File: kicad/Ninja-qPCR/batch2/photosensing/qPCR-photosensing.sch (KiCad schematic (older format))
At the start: 26 parts

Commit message: Add schematics
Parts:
- removed C? (x2): 0.1uF, symbol Device:C
- removed C?: 10pF, symbol Device:C
- removed C? (x2): 0.22uF, symbol Device:C
- removed R? (x2): 560, symbol Device:R
- removed R?: 1.1M, symbol Device:R
- removed R?: 1800, symbol Device:R
- removed U?: LME49721MAX_NOPB, M08A_TEX, symbol Ninja-qPCR:LME49721MAX_NOPB
- removed U?: Conn_02x05, symbol Ninja-qPCR:Conn_02x05
- added J?: Conn_01x10_Male, symbol Connector:Conn_01x10_Male
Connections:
- net +10V: now also J?.2 (Pin_2)
- net -10V: now also J?.3 (Pin_3)
- net GND: now also J?.1 (Pin_1)
- net PD_REF_PWM: now also J?.4 (Pin_4)
- net VCC: now also J?.8 (Pin_8)
- net ADC_IN renamed PHOTO_OUT
- net PHOTO_OUT: now also J?.9 (Pin_9)
- net MUX_SYNC renamed PD_MUX_SYNC
- net PD_MUX_SYNC: now also J?.7 (Pin_7)
- net RPI_SPI_MOSI renamed PD_MUX_SPI_MOSI
- net PD_MUX_SPI_MOSI: now also J?.6 (Pin_6)
- net RPI_SPI_SCLK renamed PD_MUX_SPI_SCLK
- net PD_MUX_SPI_SCLK: now also J?.5 (Pin_5)
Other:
- moved on the sheet: C?, R?, U?

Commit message: add schematics of test boards
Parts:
- removed C? (x2): 0.1uF, symbol Device:C
- removed C? (x2): 0.47uF, symbol Device:C
- removed J?: Conn_01x10_Male, symbol Connector:Conn_01x10_Male
- removed N_PD1, N_PD2, S_PD1, S_PD2: Conn_02x05, symbol Ninja-qPCR:Conn_02x05
- removed R? (x2): 10k, symbol Device:R
- removed R?: 6.2k, symbol Device:R
- removed R?: 1k, symbol Device:R
- removed U? (x2): ADG731BSUZ, SU_48_ADI, symbol Ninja-qPCR:ADG731BSUZ
- removed U?: AD630ARZ, RW_20_ADI, symbol Ninja-qPCR:AD630ARZ
- added C? (x2): 0.22uF, symbol Device:C
- added C?: 10pF, symbol Device:C
- added C? (x4): 0.1uF, symbol Device:C
- added C? (x2): 0.47uF, symbol Device:C
- added J?: Conn_01x15_Male, symbol Connector:Conn_01x15_Male
- added J?: Conn_01x01_Male, symbol Connector:Conn_01x01_Male
- added R? (x2): 560, symbol Device:R
- added R?: 1800, symbol Device:R
- added R?: 1.1M, symbol Device:R
- added R? (x2): 10k, symbol Device:R
- added R?: 6.2k, symbol Device:R
- added R?: 1k, symbol Device:R
- added U?: Conn_02x05, symbol Ninja-qPCR:Conn_02x05
- added U?: LME49721MAX_NOPB, M08A_TEX, symbol Ninja-qPCR:LME49721MAX_NOPB
- added U?: AD630ARZ, RW_20_ADI, symbol Ninja-qPCR:AD630ARZ
- added U?: ADS1219IPWR, PW16_TEX, symbol Ninja-qPCR:ADS1219IPWR
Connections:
- net +10V: now also C?.1, C?.1, J?.2 (Pin_2), R?.2, U?.11 (+VS), U?.2 (Pin_2), U?.8 (VDD)
- net -10V: now also C?.1, C?.1, J?.3 (Pin_3), U?.3 (Pin_3), U?.4 (VSS), U?.8 (-VS)
- net AMP_OUT: now also C?.1, R?.1, U?.1 (RINA), U?.16 (RA), U?.7 (OUT_B)
- net GND: now also C?.1, C?.2, C?.2, C?.2, C?.2, C?.2, J?.1 (Pin_1), R?.1, R?.2, U?.1 (A0), U?.1 (Pin_1), U?.14 (RB), U?.17 (RINB), U?.2 (A1), U?.3 (+IN_A), U?.4 (DGND), U?.5 (+IN_B), U?.5 (AGND), U?.8 (REFN)
- net PD_MUX_OUT: now also C?.1, R?.1, U?.2 (-IN_A), U?.5 (Pin_5)
- net PD_REF_PWM: now also J?.10 (Pin_10), U?.10 (SEL_A)
- net PHOTO_OUT: now also C?.2, R?.2, U?.11 (AIN0)
- new net: C?.2, C?.2, R?.1, R?.1
- new net: C?.1, R?.2, U?.6 (-IN_B)
- new net: C?.2, R?.2, R?.2, U?.1 (OUT_A)
- new net: R?.2, U?.12 (COMP), U?.13 (VOUT)
- new net: U?.15 (RF), U?.19 (CH_B-), U?.20 (CH_A-)
- new net: R?.1, R?.2, U?.9 (SEL_B)
- new net: C?.1, R?.1, R?.1
- new net ADC_DRDY: J?.11 (Pin_11), U?.14 (*DRDY)
- new net I2C_SCL: J?.12 (Pin_12), U?.16 (SCL)
- new net I2C_SDA: J?.13 (Pin_13), U?.15 (SDA)
- new net PD_MUX_GPIO1: J?.9 (Pin_9), U?.10 (Pin_10)
- new net PD_MUX_GPIO2: J?.8 (Pin_8), U?.9 (Pin_9)
- new net PD_MUX_GPIO3: J?.7 (Pin_7), U?.8 (Pin_8)
- new net PD_MUX_GPIO4: J?.6 (Pin_6), U?.7 (Pin_7)
- new net PD_MUX_GPIO5: J?.5 (Pin_5), U?.6 (Pin_6)
- new net THERM_AIR: J?.14 (Pin_14), U?.10 (AIN1)
- new net THERM_TEST: J?.1 (Pin_1), U?.6 (AIN3)
- new net THERM_WELL: J?.15 (Pin_15), U?.7 (AIN2)
- new net VCC_LOGIC: J?.4 (Pin_4), U?.12 (AVDD), U?.13 (DVDD), U?.3 (*RESET), U?.4 (Pin_4), U?.9 (REFP)
- no-connect marks 15 -> 7

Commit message: sync
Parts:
- removed U?: Conn_02x05, symbol Ninja-qPCR:Conn_02x05
- added J? (x2): Conn_01x05_Male, symbol Connector:Conn_01x05_Male
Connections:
- net +10V: now also J?.2 (Pin_2)
- net -10V: now also J?.3 (Pin_3)
- net GND: now also J?.1 (Pin_1)
- net PD_MUX_GPIO1: now also J?.5 (Pin_5)
- net PD_MUX_GPIO2: now also J?.4 (Pin_4)
- net PD_MUX_GPIO3: now also J?.3 (Pin_3)
- net PD_MUX_GPIO4: now also J?.2 (Pin_2)
- net PD_MUX_GPIO5: now also J?.1 (Pin_1)
- net PD_MUX_OUT: now also J?.5 (Pin_5)
- net VCC_LOGIC: now also J?.4 (Pin_4)
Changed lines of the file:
@@
 Comment4 ""
 $EndDescr
-Text GLabel 10000 5300 2    50   Input ~ 0
-GND
-Text GLabel 10000 5400 2    50   Input ~ 0
+Text GLabel 8800 4650 2    50   Input ~ 0
+GND
+Text GLabel 8800 4750 2    50   Input ~ 0
 +10V
-Text GLabel 10000 5500 2    50   Input ~ 0
+Text GLabel 8800 4850 2    50   Input ~ 0
 -10V
 Wire Wire Line
-	9800 5300 10000 5300
-Wire Wire Line
-	10000 5400 9800 5400
-Wire Wire Line
-	9800 5500 10000 5500
-Wire Wire Line
-	10000 5600 9800 5600
-Wire Wire Line
-	9800 5700 10000 5700
-Wire Wire Line
-	10000 5800 9800 5800
-Wire Wire Line
-	9800 5900 10000 5900
-Wire Wire Line
-	10000 6000 9800 6000
-Wire Wire Line
-	9800 6100 10000 6100
-$Comp
-L Ninja-qPCR:Conn_02x05 U?
-U 1 1 5F51FB4B
-P 9600 5300
-F 0 "U?" H 9919 4911 50  0000 L CNN
-F 1 "Conn_02x05" H 9919 4820 50  0000 L CNN
-F 2 "" H 9400 5400 50  0001 C CNN
-F 3 "" H 9400 5400 50  0001 C CNN
-	1    9600 5300
-	-1   0    0    -1
-$EndComp
-Wire Wire Line
-	10000 6200 9800 6200
-Text GLabel 10000 5600 2    50   Input ~ 0
+	8600 4650 8800 4650
+Wire Wire Line
+	8800 4750 8600 4750
+Wire Wire Line
+	8600 4850 8800 4850
+Wire Wire Line
+	8800 4950 8600 4950
+Wire Wire Line
+	8600 5050 8800 5050
+Wire Wire Line
+	8800 5350 8600 5350
+Wire Wire Line
+	8600 5450 8800 5450
+Wire Wire Line
+	8800 5550 8600 5550
+Wire Wire Line
+	8600 5650 8800 5650
+Wire Wire Line
+	8800 5750 8600 5750
+Text GLabel 8800 4950 2    50   Input ~ 0
 VCC_LOGIC
-Text GLabel 10000 5700 2    50   Input ~ 0
+Text GLabel 8800 5050 2    50   Input ~ 0
 PD_MUX_OUT
-Text GLabel 10000 6200 2    50   Input ~ 0
+Text GLabel 8800 5750 2    50   Input ~ 0
 PD_MUX_GPIO1
-Text GLabel 10000 6100 2    50   Input ~ 0
+Text GLabel 8800 5650 2    50   Input ~ 0
 PD_MUX_GPIO2
-Text GLabel 10000 6000 2    50   Input ~ 0
+Text GLabel 8800 5550 2    50   Input ~ 0
 PD_MUX_GPIO3
-Text GLabel 10000 5900 2    50   Input ~ 0
+Text GLabel 8800 5450 2    50   Input ~ 0
 PD_MUX_GPIO4
-Text GLabel 10000 5800 2    50   Input ~ 0
+Text GLabel 8800 5350 2    50   Input ~ 0
 PD_MUX_GPIO5
 Text GLabel 1350 850  2    50   Input ~ 0
@@
 Text HLabel 7400 4250 2    50   Input ~ 0
 PHOTO_OUT
+$Comp
+L Connector:Conn_01x05_Male J?
+U 1 1 5F591AD7
+P 8400 4850
+F 0 "J?" H 8508 5231 50  0000 C CNN
+F 1 "Conn_01x05_Male" H 8508 5140 50  0000 C CNN
+F 2 "" H 8400 4850 50  0001 C CNN
+F 3 "~" H 8400 4850 50  0001 C CNN
+	1    8400 4850
+	1    0    0    -1
+$EndComp
+$Comp
+L Connector:Conn_01x05_Male J?
+U 1 1 5F59281D
+P 8400 5550
+F 0 "J?" H 8508 5931 50  0000 C CNN
+F 1 "Conn_01x05_Male" H 8508 5840 50  0000 C CNN
+F 2 "" H 8400 5550 50  0001 C CNN
+F 3 "~" H 8400 5550 50  0001 C CNN
+	1    8400 5550
+	1    0    0    -1
+$EndComp
 $EndSCHEMATC

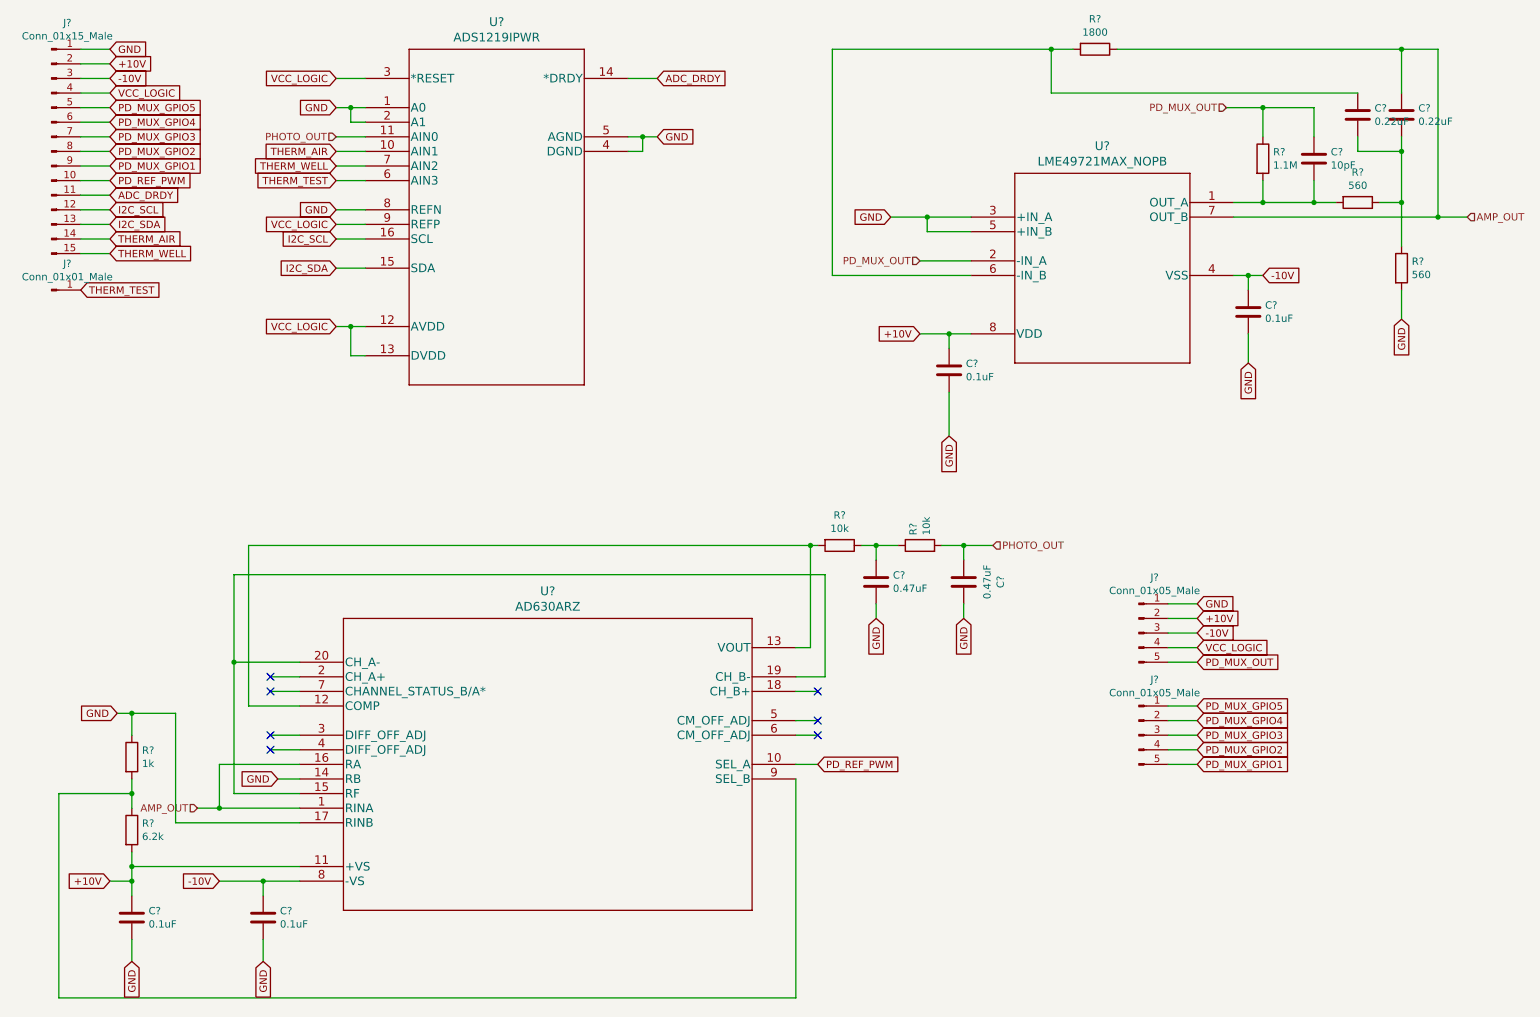
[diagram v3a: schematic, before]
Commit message: wire photosensing
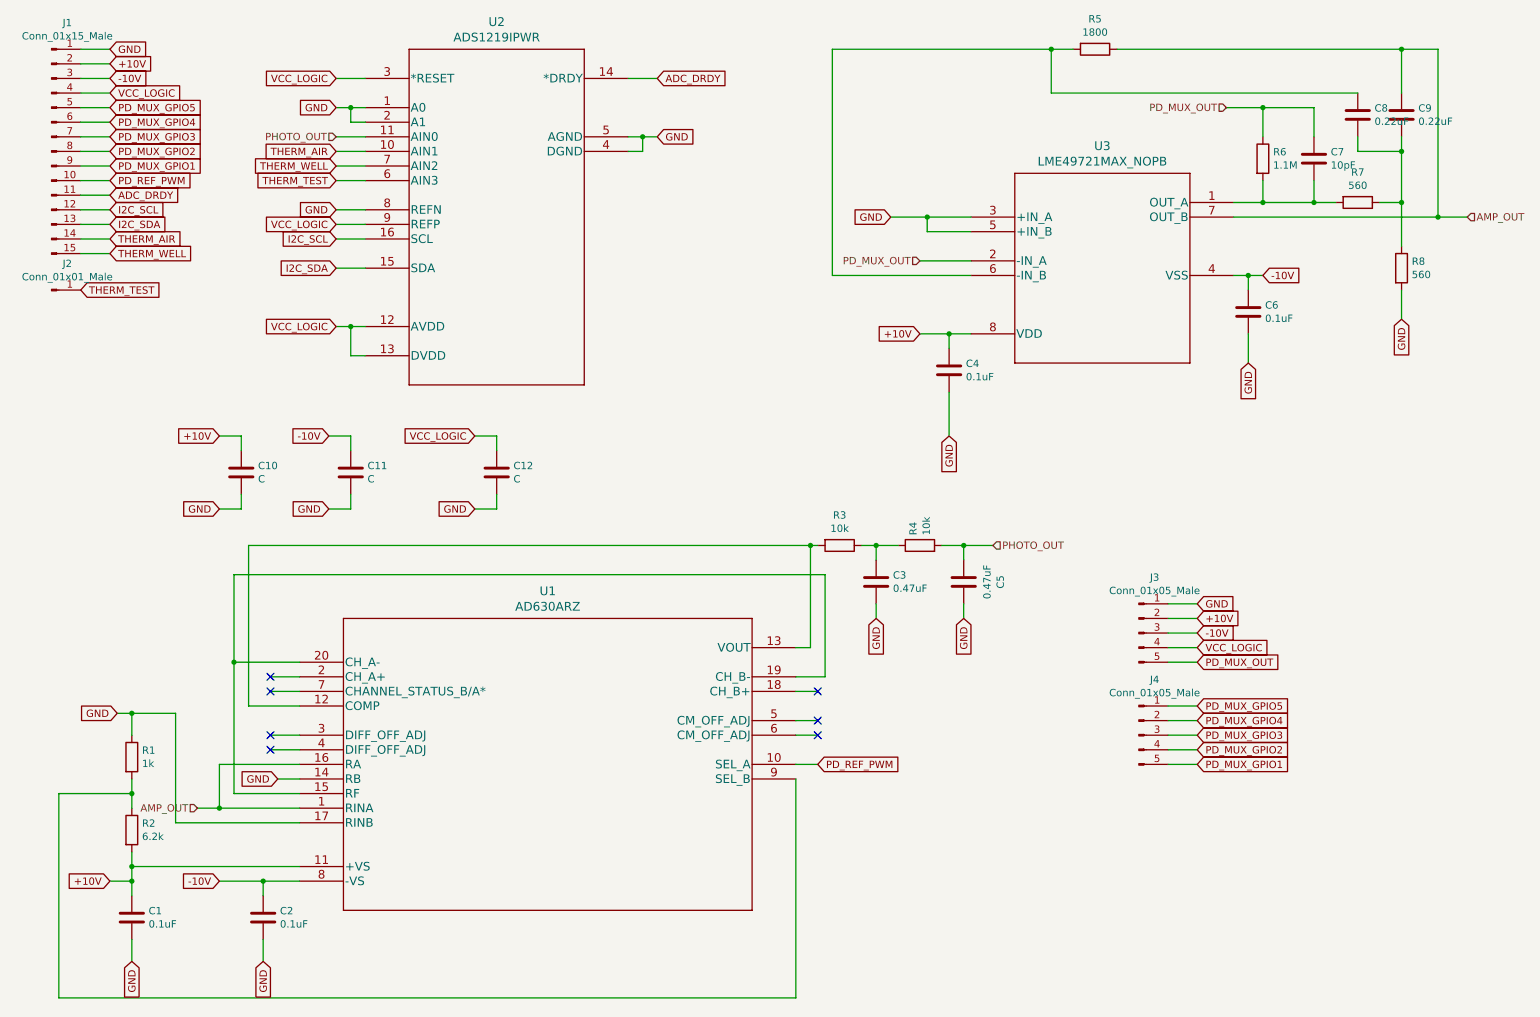
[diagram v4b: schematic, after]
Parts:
- added C10, C11, C12: C, Capacitors_SMD:C_0805_HandSoldering, symbol Device:C
- C1, C2, C4, C6: renamed from C?; footprint (none) -> Resistors_SMD:R_0603_HandSoldering
- C3, C5, C8, C9: renamed from C?; footprint (none) -> Resistors_SMD:R_1206_HandSoldering
- C7: renamed from C?; footprint (none) -> Capacitors_ThroughHole:C_Disc_D3.0mm_W2.0mm_P2.50mm
- J1: renamed from J?; footprint (none) -> Pin_Headers:Pin_Header_Angled_1x15_Pitch2.54mm
- J2: renamed from J?; footprint (none) -> Pin_Headers:Pin_Header_Straight_1x01_Pitch2.54mm
- J3, J4: renamed from J?; footprint (none) -> Pin_Headers:Pin_Header_Straight_1x05_Pitch2.54mm
- R1, R2, R3, R4, R5, R6, R7, R8: renamed from R?; footprint (none) -> Resistors_SMD:R_0603_HandSoldering
- U1: renamed from U?; footprint RW_20_ADI -> Ninja-qPCR:AD630ARZ
- U2: renamed from U?; footprint PW16_TEX -> Ninja-qPCR:ADS1219IPWR
- U3: renamed from U?; footprint M08A_TEX -> Ninja-qPCR:LME49721MAX&slash_NOPB
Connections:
- net +10V: now also C10.1
- net -10V: now also C11.1
- net GND: now also C10.2, C11.2, C12.2
- net VCC_LOGIC: now also C12.1

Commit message: add LTC
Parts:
- removed J1: Conn_01x15_Male, Pin_Headers:Pin_Header_Angled_1x15_Pitch2.54mm, symbol Connector:Conn_01x15_Male
- removed J2: Conn_01x01_Male, Pin_Headers:Pin_Header_Straight_1x01_Pitch2.54mm, symbol Connector:Conn_01x01_Male
- added J1: Conn_01x14_Male, Pin_Headers:Pin_Header_Angled_1x14_Pitch2.54mm, symbol Connector:Conn_01x14_Male
- added J2: Conn_01x02_Male, Pin_Headers:Pin_Header_Straight_1x02_Pitch2.54mm, symbol Connector:Conn_01x02_Male
- renumbered C7 to C10, C8 to C11, C9 to C12, C10 to C2, C2 to C3, C11 to C4, C12 to C5, C3 to C6, C4 to C7, C5 to C8, C6 to C9
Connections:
- net THERM_AIR is gone; now on net THERM_WELL: U2.10 (AIN1)
- net +10V: now also J1.2 (Pin_2)
- net -10V: now also J1.3 (Pin_3)
- net ADC_DRDY: now also J1.11 (Pin_11)
- net GND: now also J1.1 (Pin_1)
- net I2C_SCL: now also J1.12 (Pin_12)
- net I2C_SDA: now also J1.13 (Pin_13)
- net PD_MUX_GPIO1: now also J1.9 (Pin_9)
- net PD_MUX_GPIO2: now also J1.8 (Pin_8)
- net PD_MUX_GPIO3: now also J1.7 (Pin_7)
- net PD_MUX_GPIO4: now also J1.6 (Pin_6)
- net PD_MUX_GPIO5: now also J1.5 (Pin_5)
- net PD_REF_PWM: now also J1.10 (Pin_10)
- net THERM_WELL: now also J1.14 (Pin_14); no longer U2.7 (AIN2)
- net VCC_LOGIC: now also J1.4 (Pin_4)
- net THERM_TEST renamed THERM_TEST2
- net THERM_TEST2: now also J2.2 (Pin_2)
- new net THERM_TEST1: J2.1 (Pin_1), U2.7 (AIN2)
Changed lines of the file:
@@
 Text GLabel 2900 1250 0    50   Input ~ 0
 GND
-Text GLabel 2900 1550 0    50   Input ~ 0
-THERM_AIR
 Text HLabel 2900 1450 0    50   Input ~ 0
 PHOTO_OUT
+Text GLabel 2900 1550 0    50   Input ~ 0
+THERM_WELL
 Text GLabel 2900 1650 0    50   Input ~ 0
-THERM_WELL
-Text GLabel 2900 1750 0    50   Input ~ 0
-THERM_TEST
+THERM_TEST1
 Text GLabel 2900 1950 0    50   Input ~ 0
 GND
@@
 Wire Wire Line
 	5000 1450 4900 1450
-Text GLabel 1150 2500 2    50   Input ~ 0
-THERM_TEST
+Text GLabel 1350 2550 2    50   Input ~ 0
+THERM_TEST1
 Text GLabel 1350 1850 2    50   Input ~ 0
 ADC_DRDY
@@
 	1350 2050 1150 2050
 Text GLabel 1350 2150 2    50   Input ~ 0
-THERM_AIR
-Text GLabel 1350 2250 2    50   Input ~ 0
 THERM_WELL
-$Comp
-L Connector:Conn_01x15_Male J1
-U 1 1 5F575969
-P 950 1550
-F 0 "J1" H 1058 2431 50  0000 C CNN
-F 1 "Conn_01x15_Male" H 1058 2340 50  0000 C CNN
-F 2 "Pin_Headers:Pin_Header_Angled_1x15_Pitch2.54mm" H 950 1550 50  0001 C CNN
-F 3 "~" H 950 1550 50  0001 C CNN
-	1    950  1550
-	1    0    0    -1
-$EndComp
 Wire Wire Line
 	1350 2150 1150 2150
-Wire Wire Line
-	1350 2250 1150 2250
-$Comp
-L Connector:Conn_01x01_Male J2
-U 1 1 5F577405
-P 950 2500
-F 0 "J2" H 1058 2681 50  0000 C CNN
-F 1 "Conn_01x01_Male" H 1058 2590 50  0000 C CNN
-F 2 "Pin_Headers:Pin_Header_Straight_1x01_Pitch2.54mm" H 950 2500 50  0001 C CNN
-F 3 "~" H 950 2500 50  0001 C CNN
-	1    950  2500
-	1    0    0    -1
-$EndComp
 Text GLabel 7100 3500 3    50   Input ~ 0
 GND
@@
 P 10200 1300
 AR Path="/5F4A628B/5F581541" Ref="C?"  Part="1"
-AR Path="/5F581541" Ref="C9"  Part="1"
+AR Path="/5F581541" Ref="C12"  Part="1"
 AR Path="/5F620C27/5F581541" Ref="C?"  Part="1"
-F 0 "C9" H 10315 1346 50  0000 L CNN
+F 0 "C12" H 10315 1346 50  0000 L CNN
 F 1 "0.22uF" H 10315 1255 50  0000 L CNN
 F 2 "Resistors_SMD:R_1206_HandSoldering" H 10238 1150 50  0001 C CNN
@@
 P 9900 1300
 AR Path="/5F4A628B/5F581547" Ref="C?"  Part="1"
-AR Path="/5F581547" Ref="C8"  Part="1"
+AR Path="/5F581547" Ref="C11"  Part="1"
 AR Path="/5F620C27/5F581547" Ref="C?"  Part="1"
-F 0 "C8" H 10015 1346 50  0000 L CNN
+F 0 "C11" H 10015 1346 50  0000 L CNN
 F 1 "0.22uF" H 10015 1255 50  0000 L CNN
 F 2 "Resistors_SMD:R_1206_HandSoldering" H 9938 1150 50  0001 C CNN
@@
 P 9600 1600
 AR Path="/5F4A628B/5F58156F" Ref="C?"  Part="1"
-AR Path="/5F58156F" Ref="C7"  Part="1"
+AR Path="/5F58156F" Ref="C10"  Part="1"
 AR Path="/5F620C27/5F58156F" Ref="C?"  Part="1"
-F 0 "C7" H 9715 1646 50  0000 L CNN
+F 0 "C10" H 9715 1646 50  0000 L CNN
 F 1 "10pF" H 9715 1555 50  0000 L CNN
 F 2 "Capacitors_ThroughHole:C_Disc_D3.0mm_W2.0mm_P2.50mm" H 9638 1450 50  0001 C CNN
@@
 P 9150 2650
 AR Path="/5F4A628B/5F581587" Ref="C?"  Part="1"
-AR Path="/5F581587" Ref="C6"  Part="1"
+AR Path="/5F581587" Ref="C9"  Part="1"
 AR Path="/5F620C27/5F581587" Ref="C?"  Part="1"
-F 0 "C6" H 9265 2696 50  0000 L CNN
+F 0 "C9" H 9265 2696 50  0000 L CNN
 F 1 "0.1uF" H 9265 2605 50  0000 L CNN
 F 2 "Resistors_SMD:R_0603_HandSoldering" H 9188 2500 50  0001 C CNN
@@
 P 7100 3050
 AR Path="/5F4A628B/5F581592" Ref="C?"  Part="1"
-AR Path="/5F581592" Ref="C4"  Part="1"
+AR Path="/5F581592" Ref="C7"  Part="1"
 AR Path="/5F620C27/5F581592" Ref="C?"  Part="1"
-F 0 "C4" H 7215 3096 50  0000 L CNN
+F 0 "C7" H 7215 3096 50  0000 L CNN
 F 1 "0.1uF" H 7215 3005 50  0000 L CNN
 F 2 "Resistors_SMD:R_0603_HandSoldering" H 7138 2900 50  0001 C CNN
@@
 	2650 6550 2400 6550
 $Comp
-L Device:C C2
+L Device:C C3
 U 1 1 5F58E360
 P 2400 6800
-F 0 "C2" H 2515 6846 50  0000 L CNN
+F 0 "C3" H 2515 6846 50  0000 L CNN
 F 1 "0.1uF" H 2515 6755 50  0000 L CNN
 F 2 "Resistors_SMD:R_0603_HandSoldering" H 2438 6650 50  0001 C CNN
@@
 Connection ~ 1500 5400
 $Comp
-L Device:C C3
+L Device:C C6
 U 1 1 5F58E395
 P 6600 4500
-F 0 "C3" H 6715 4546 50  0000 L CNN
+F 0 "C6" H 6715 4546 50  0000 L CNN
 F 1 "0.47uF" H 6715 4455 50  0000 L CNN
 F 2 "Resistors_SMD:R_1206_HandSoldering" H 6638 4350 50  0001 C CNN
@@
 $EndComp
 $Comp
-L Device:C C5
+L Device:C C8
 U 1 1 5F58E3A5
 P 7200 4500
-F 0 "C5" V 6948 4500 50  0000 C CNN
+F 0 "C8" V 6948 4500 50  0000 C CNN
 F 1 "0.47uF" V 7039 4500 50  0000 C CNN
 F 2 "Resistors_SMD:R_1206_HandSoldering" H 7238 4350 50  0001 C CNN
@@
 GND
 $Comp
-L Device:C C10
+L Device:C C2
 U 1 1 5F5B08B9
 P 2250 3750
-F 0 "C10" H 2365 3796 50  0000 L CNN
+F 0 "C2" H 2365 3796 50  0000 L CNN
 F 1 "C" H 2365 3705 50  0000 L CNN
 F 2 "Capacitors_SMD:C_0805_HandSoldering" H 2288 3600 50  0001 C CNN
@@
 $EndComp
 $Comp
-L Device:C C11
+L Device:C C4
 U 1 1 5F5B10F8
 P 3000 3750
-F 0 "C11" H 3115 3796 50  0000 L CNN
+F 0 "C4" H 3115 3796 50  0000 L CNN
 F 1 "C" H 3115 3705 50  0000 L CNN
 F 2 "Capacitors_SMD:C_0805_HandSoldering" H 3038 3600 50  0001 C CNN
@@
 $EndComp
 $Comp
-L Device:C C12
+L Device:C C5
 U 1 1 5F5B161D
 P 4000 3750
-F 0 "C12" H 4115 3796 50  0000 L CNN
+F 0 "C5" H 4115 3796 50  0000 L CNN
 F 1 "C" H 4115 3705 50  0000 L CNN
 F 2 "Capacitors_SMD:C_0805_HandSoldering" H 4038 3600 50  0001 C CNN
@@
 Wire Wire Line
 	2250 3900 2250 4000
+$Comp
+L Connector:Conn_01x14_Male J1
+U 1 1 5F5FEB48
+P 950 1450
+F 0 "J1" H 1058 2231 50  0000 C CNN
+F 1 "Conn_01x14_Male" H 1058 2140 50  0000 C CNN
+F 2 "Pin_Headers:Pin_Header_Angled_1x14_Pitch2.54mm" H 950 1450 50  0001 C CNN
+F 3 "~" H 950 1450 50  0001 C CNN
+	1    950  1450
+	1    0    0    -1
+$EndComp
+$Comp
+L Connector:Conn_01x02_Male J2
+U 1 1 5F602441
+P 950 2550
+F 0 "J2" H 1058 2731 50  0000 C CNN
+F 1 "Conn_01x02_Male" H 1058 2640 50  0000 C CNN
+F 2 "Pin_Headers:Pin_Header_Straight_1x02_Pitch2.54mm" H 950 2550 50  0001 C CNN
+F 3 "~" H 950 2550 50  0001 C CNN
+	1    950  2550
+	1    0    0    -1
+$EndComp
+Text GLabel 1350 2650 2    50   Input ~ 0
+THERM_TEST2
+Wire Wire Line
+	1350 2550 1150 2550
+Wire Wire Line
+	1350 2650 1150 2650
+Text GLabel 2900 1750 0    50   Input ~ 0
+THERM_TEST2
 $EndSCHEMATC
